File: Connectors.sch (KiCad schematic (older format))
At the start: 4 parts, among them J1 Serial Port, J2 Digital pins, J3 I2C, J4 ISCP

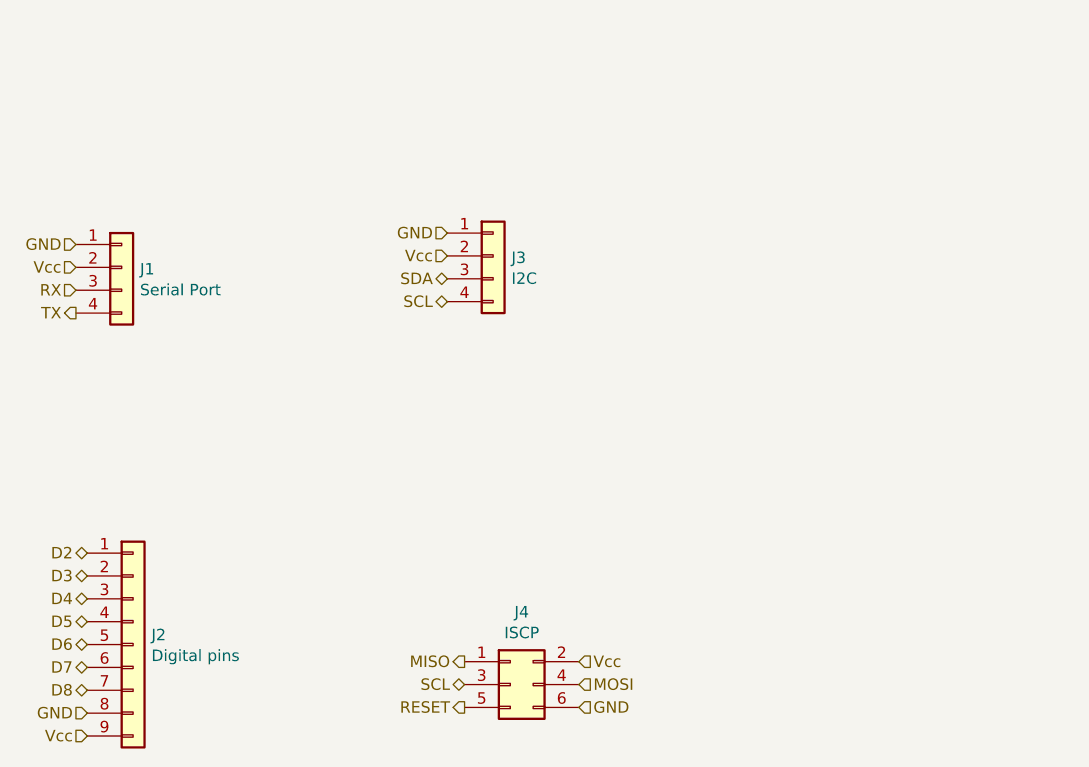
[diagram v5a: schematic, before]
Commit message: Added functional blocks and comments.
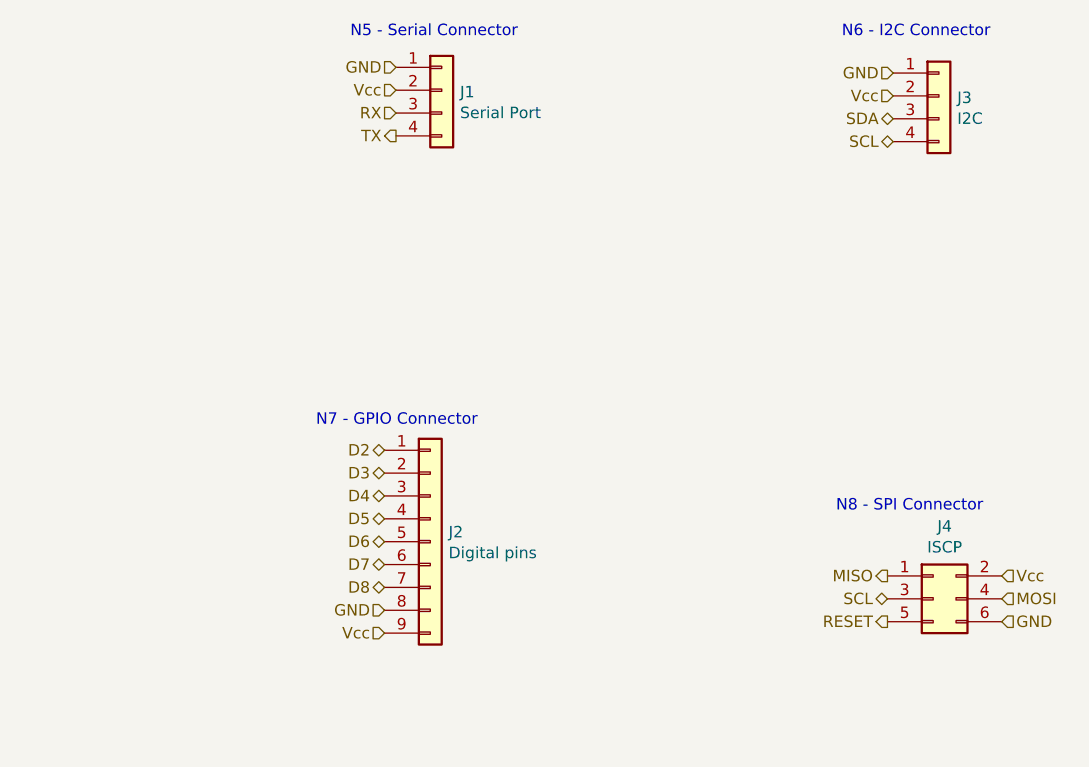
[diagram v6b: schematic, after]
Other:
- note added: "N5 - Serial Connector"
- note added: "N6 - I2C Connector"
- note added: "N7 - GPIO Connector"
- note added: "N8 - SPI Connector"
- moved on the sheet: J1, J2, J3, J4
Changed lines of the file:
@@
 L Connector_Generic:Conn_01x09 J2
 U 1 1 60D7775B
-P 3325 4650
-F 0 "J2" H 3405 4692 50  0000 L CNN
-F 1 "Digital pins" H 3405 4601 50  0000 L CNN
-F 2 "Connector_PinHeader_2.54mm:PinHeader_1x09_P2.54mm_Vertical" H 3325 4650 50  0001 C CNN
-F 3 "~" H 3325 4650 50  0001 C CNN
-	1    3325 4650
+P 4625 4200
+F 0 "J2" H 4705 4242 50  0000 L CNN
+F 1 "Digital pins" H 4705 4151 50  0000 L CNN
+F 2 "Connector_PinHeader_2.54mm:PinHeader_1x09_P2.54mm_Vertical" H 4625 4200 50  0001 C CNN
+F 3 "~" H 4625 4200 50  0001 C CNN
+	1    4625 4200
 	1    0    0    -1
 $EndComp
@@
 L Connector_Generic:Conn_01x04 J1
 U 1 1 60D7857C
-P 3275 3000
-F 0 "J1" H 3355 2992 50  0000 L CNN
-F 1 "Serial Port" H 3355 2901 50  0000 L CNN
-F 2 "Connector_PinHeader_2.54mm:PinHeader_1x04_P2.54mm_Vertical" H 3275 3000 50  0001 C CNN
-F 3 "~" H 3275 3000 50  0001 C CNN
-	1    3275 3000
+P 4675 2225
+F 0 "J1" H 4755 2217 50  0000 L CNN
+F 1 "Serial Port" H 4755 2126 50  0000 L CNN
+F 2 "Connector_PinHeader_2.54mm:PinHeader_1x04_P2.54mm_Vertical" H 4675 2225 50  0001 C CNN
+F 3 "~" H 4675 2225 50  0001 C CNN
+	1    4675 2225
 	1    0    0    -1
 $EndComp
@@
 L Connector_Generic:Conn_01x04 J3
 U 1 1 60D78A32
-P 4900 2950
-F 0 "J3" H 4980 2942 50  0000 L CNN
-F 1 "I2C" H 4980 2851 50  0000 L CNN
-F 2 "Connector_PinHeader_2.54mm:PinHeader_1x04_P2.54mm_Vertical" H 4900 2950 50  0001 C CNN
-F 3 "~" H 4900 2950 50  0001 C CNN
-	1    4900 2950
+P 6850 2250
+F 0 "J3" H 6930 2242 50  0000 L CNN
+F 1 "I2C" H 6930 2151 50  0000 L CNN
+F 2 "Connector_PinHeader_2.54mm:PinHeader_1x04_P2.54mm_Vertical" H 6850 2250 50  0001 C CNN
+F 3 "~" H 6850 2250 50  0001 C CNN
+	1    6850 2250
 	1    0    0    -1
 $EndComp
@@
 L Connector_Generic:Conn_02x03_Odd_Even J4
 U 1 1 60D796C8
-P 4975 4825
-F 0 "J4" H 5025 5142 50  0000 C CNN
-F 1 "ISCP" H 5025 5051 50  0000 C CNN
-F 2 "Connector_PinHeader_2.54mm:PinHeader_2x03_P2.54mm_Vertical" H 4975 4825 50  0001 C CNN
-F 3 "~" H 4975 4825 50  0001 C CNN
-	1    4975 4825
+P 6825 4450
+F 0 "J4" H 6875 4767 50  0000 C CNN
+F 1 "ISCP" H 6875 4676 50  0000 C CNN
+F 2 "Connector_PinHeader_2.54mm:PinHeader_2x03_P2.54mm_Vertical" H 6825 4450 50  0001 C CNN
+F 3 "~" H 6825 4450 50  0001 C CNN
+	1    6825 4450
 	1    0    0    -1
 $EndComp
-Text HLabel 4775 4725 0    50   Output ~ 0
+Text HLabel 6625 4350 0    50   Output ~ 0
 MISO
-Text HLabel 4775 4825 0    50   BiDi ~ 0
+Text HLabel 6625 4450 0    50   BiDi ~ 0
 SCL
-Text HLabel 4775 4925 0    50   Output ~ 0
+Text HLabel 6625 4550 0    50   Output ~ 0
 RESET
-Text HLabel 5275 4725 2    50   Input ~ 0
+Text HLabel 7125 4350 2    50   Input ~ 0
 Vcc
-Text HLabel 5275 4825 2    50   Input ~ 0
+Text HLabel 7125 4450 2    50   Input ~ 0
 MOSI
-Text HLabel 5275 4925 2    50   Input ~ 0
+Text HLabel 7125 4550 2    50   Input ~ 0
 GND
-Text HLabel 3075 2900 0    50   Input ~ 0
+Text HLabel 4475 2125 0    50   Input ~ 0
 GND
-Text HLabel 3075 3000 0    50   Input ~ 0
+Text HLabel 4475 2225 0    50   Input ~ 0
 Vcc
-Text HLabel 3075 3100 0    50   Input ~ 0
+Text HLabel 4475 2325 0    50   Input ~ 0
 RX
-Text HLabel 3075 3200 0    50   Output ~ 0
+Text HLabel 4475 2425 0    50   Output ~ 0
 TX
-Text HLabel 4700 2850 0    50   Input ~ 0
+Text HLabel 6650 2150 0    50   Input ~ 0
 GND
-Text HLabel 4700 2950 0    50   Input ~ 0
+Text HLabel 6650 2250 0    50   Input ~ 0
 Vcc
-Text HLabel 4700 3050 0    50   BiDi ~ 0
+Text HLabel 6650 2350 0    50   BiDi ~ 0
 SDA
-Text HLabel 4700 3150 0    50   BiDi ~ 0
+Text HLabel 6650 2450 0    50   BiDi ~ 0
 SCL
-Text HLabel 3125 4250 0    50   BiDi ~ 0
+Text HLabel 4425 3800 0    50   BiDi ~ 0
 D2
-Text HLabel 3125 4350 0    50   BiDi ~ 0
+Text HLabel 4425 3900 0    50   BiDi ~ 0
 D3
-Text HLabel 3125 4450 0    50   BiDi ~ 0
+Text HLabel 4425 4000 0    50   BiDi ~ 0
 D4
-Text HLabel 3125 4550 0    50   BiDi ~ 0
+Text HLabel 4425 4100 0    50   BiDi ~ 0
 D5
-Text HLabel 3125 4650 0    50   BiDi ~ 0
+Text HLabel 4425 4200 0    50   BiDi ~ 0
 D6
-Text HLabel 3125 4750 0    50   BiDi ~ 0
+Text HLabel 4425 4300 0    50   BiDi ~ 0
 D7
-Text HLabel 3125 4850 0    50   BiDi ~ 0
+Text HLabel 4425 4400 0    50   BiDi ~ 0
 D8
-Text HLabel 3125 4950 0    50   Input ~ 0
+Text HLabel 4425 4500 0    50   Input ~ 0
 GND
-Text HLabel 3125 5050 0    50   Input ~ 0
+Text HLabel 4425 4600 0    50   Input ~ 0
 Vcc
+Text Notes 4275 2000 0    50   ~ 0
+N5 - Serial Connector
+Text Notes 6425 2000 0    50   ~ 0
+N6 - I2C Connector
+Text Notes 4125 3700 0    50   ~ 0
+N7 - GPIO Connector
+Text Notes 6400 4075 0    50   ~ 0
+N8 - SPI Connector
 $EndSCHEMATC

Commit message: Changed pin headers to pin sockets where necessary.
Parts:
- J1, J3: footprint Connector_PinHeader_2.54mm:PinHeader_1x04_P2.54mm_Vertical -> Connector_PinSocket_2.54mm:PinSocket_1x04_P2.54mm_Vertical
- J2: footprint Connector_PinHeader_2.54mm:PinHeader_1x09_P2.54mm_Vertical -> Connector_PinSocket_2.54mm:PinSocket_1x09_P2.54mm_Vertical
- J4: footprint Connector_PinHeader_2.54mm:PinHeader_2x03_P2.54mm_Vertical -> Connector_PinSocket_2.54mm:PinSocket_2x03_P2.54mm_Vertical
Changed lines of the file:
@@
 F 0 "J2" H 4705 4242 50  0000 L CNN
 F 1 "Digital pins" H 4705 4151 50  0000 L CNN
-F 2 "Connector_PinHeader_2.54mm:PinHeader_1x09_P2.54mm_Vertical" H 4625 4200 50  0001 C CNN
+F 2 "Connector_PinSocket_2.54mm:PinSocket_1x09_P2.54mm_Vertical" H 4625 4200 50  0001 C CNN
 F 3 "~" H 4625 4200 50  0001 C CNN
 	1    4625 4200
@@
 F 0 "J1" H 4755 2217 50  0000 L CNN
 F 1 "Serial Port" H 4755 2126 50  0000 L CNN
-F 2 "Connector_PinHeader_2.54mm:PinHeader_1x04_P2.54mm_Vertical" H 4675 2225 50  0001 C CNN
+F 2 "Connector_PinSocket_2.54mm:PinSocket_1x04_P2.54mm_Vertical" H 4675 2225 50  0001 C CNN
 F 3 "~" H 4675 2225 50  0001 C CNN
 	1    4675 2225
@@
 F 0 "J3" H 6930 2242 50  0000 L CNN
 F 1 "I2C" H 6930 2151 50  0000 L CNN
-F 2 "Connector_PinHeader_2.54mm:PinHeader_1x04_P2.54mm_Vertical" H 6850 2250 50  0001 C CNN
+F 2 "Connector_PinSocket_2.54mm:PinSocket_1x04_P2.54mm_Vertical" H 6850 2250 50  0001 C CNN
 F 3 "~" H 6850 2250 50  0001 C CNN
 	1    6850 2250
@@
 F 0 "J4" H 6875 4767 50  0000 C CNN
 F 1 "ISCP" H 6875 4676 50  0000 C CNN
-F 2 "Connector_PinHeader_2.54mm:PinHeader_2x03_P2.54mm_Vertical" H 6825 4450 50  0001 C CNN
+F 2 "Connector_PinSocket_2.54mm:PinSocket_2x03_P2.54mm_Vertical" H 6825 4450 50  0001 C CNN
 F 3 "~" H 6825 4450 50  0001 C CNN
 	1    6825 4450
